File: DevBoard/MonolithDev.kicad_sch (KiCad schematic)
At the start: 4 parts

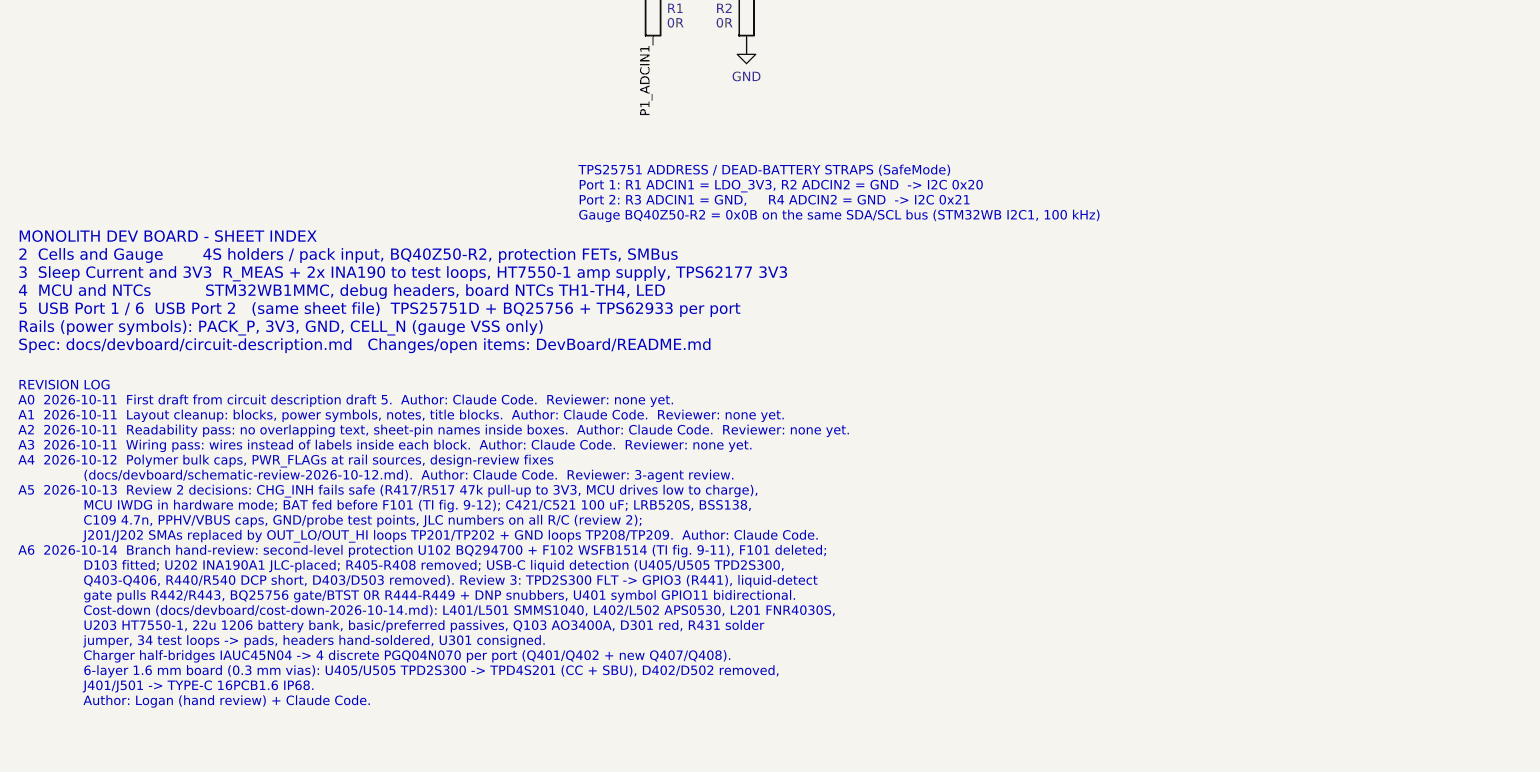
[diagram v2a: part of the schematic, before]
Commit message: Dev board schematic: tidy pass
- Title blocks on every sheet: rev A6, 2026-10-14, status line updated
  (was "Not reviewed, laid out, built or tested"); tidy_fields.py
  writes the same.
- Port sheet: the TPD4S201 block is titled with liquid detection
  ("CC/SBU PROTECTION (TPD4S201) + LIQUID DETECTION") and moved clear of
  the heading it collided with; I2Cc heading moved next to the EEPROM;
  PP5V heading clear of U405's GND.
- MCU sheet: test-point row out of the title block, with a heading;
  long NOTES lines wrapped inside the page border.
- Gauge sheet: cell-stack heading clear of its note; TP106 joins the
  test-point row.
- Top sheet: sheet index updated (BQ294700, TPD4S201, TH1-TH5) and
  spaced from the strap note and revision log; rev log line for the
  placement and this tidy.
- New tools/move_region.py moves a rectangle of a sheet (symbols,
  fields, wires, labels) by an offset.

Netlist identical before and after (265 nets); ERC 0 errors;
check_overlaps TOTAL 0.

Co-Authored-By: Claude Opus 5.5 <noreply@anthropic.com>
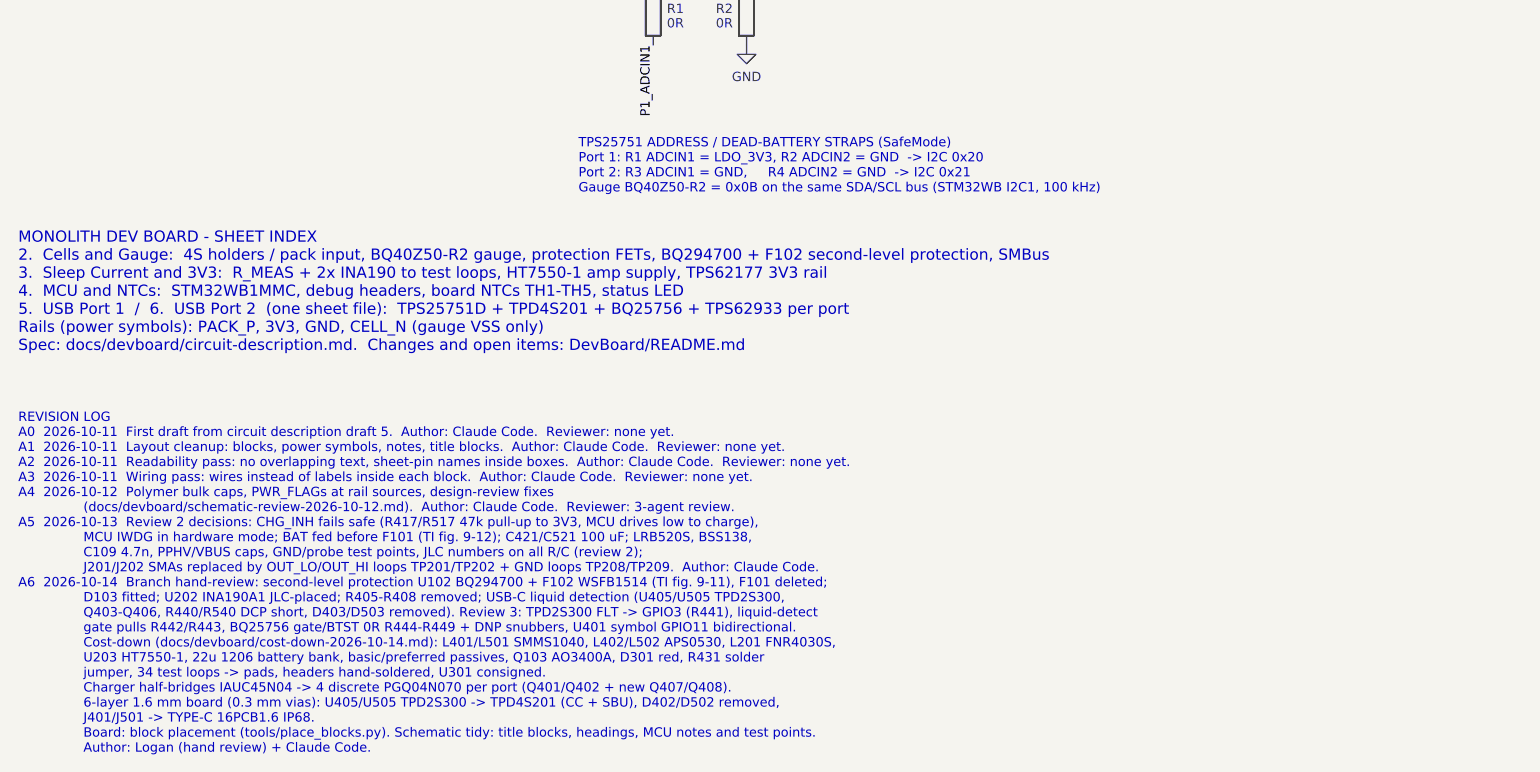
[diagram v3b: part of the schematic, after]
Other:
- note added: "MONOLITH DEV BOARD - SHEET INDEX 2. Cells and Gauge: 4S holders / pack input, BQ40Z50-R2 gauge, protection FETs, BQ294700 + F102 second-level protection, SMBus 3. Sleep Current and 3V3: R_MEAS + 2x INA190 to test loops, HT7550-1 amp supply, TPS62177 3V3 rail 4. MCU and NTCs: STM32WB1MMC, debug headers, board NTCs TH1-TH5, status LED 5. USB Port 1 / 6. USB Port 2 (one sheet file): TPS25751D + TPD4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"
- note removed: "MONOLITH DEV BOARD - SHEET INDEX 2 Cells and Gauge 4S holders / pack input, BQ40Z50-R2, protection FETs, SMBus 3 Sleep Current and 3V3 R_MEAS + 2x INA190 to test loops, HT7550-1 amp supply, TPS62177 3V3 4 MCU and NTCs STM32WB1MMC, debug headers, board NTCs TH1-TH4, LED 5 USB Port 1 / 6 USB Port 2 (same sheet file) TPS25751D + BQ25756 + TPS62933 per port Rails (power symbols): PACK_P, 3V3, GND, CE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"
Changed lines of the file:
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@@
 	(title_block
 		(title "Monolith dev board - top level")
-		(date "2026-10-11")
-		(rev "A (draft)")
+		(date "2026-10-14")
+		(rev "A6")
 		(company "Monolith 100 W battery bank - dev board")
 		(comment 1 "Sheet index, PD address straps")
 		(comment 2 "Spec + open items: DevBoard/README.md")
-		(comment 3 "Not reviewed, laid out, built or tested")
+		(comment 3 "Reviewed 3x (docs/devboard); board placed, not routed or built")
 	)
-	(text "MONOLITH DEV BOARD - SHEET INDEX\n2  Cells and Gauge        4S holders / pack input, BQ40Z50-R2, protection FETs, SMBus\n3  Sleep Current and 3V3  R_MEAS + 2x INA190 to test loops, HT7550-1 amp supply, TPS62177 3V3\n4  MCU and NTCs           STM32WB1MMC, debug headers, board NTCs TH1-TH4, LED\n5  USB Port 1 / 6  USB Port 2   (same sheet file)  TPS25751D + BQ25756 + TPS62933 per port\nRails (power symbols): PACK_P, 3V3, GND, CELL_N (gauge VSS only)\nSpec: docs/devboard/circuit-description.md   Changes/open items: DevBoard/README.md"
+	(text "MONOLITH DEV BOARD - SHEET INDEX\n2.  Cells and Gauge:  4S holders / pack input, BQ40Z50-R2 gauge, protection FETs, BQ294700 + F102 second-level protection, SMBus\n3.  Sleep Current and 3V3:  R_MEAS + 2x INA190 to test loops, HT7550-1 amp supply, TPS62177 3V3 rail\n4.  MCU and NTCs:  STM32WB1MMC, debug headers, board NTCs TH1-TH5, status LED\n5.  USB Port 1  /  6.  USB Port 2  (one sheet file):  TPS25751D + TPD4S201 + BQ25756 + TPS62933 per port\nRails (power symbols): PACK_P, 3V3, GND, CELL_N (gauge VSS only)\nSpec: docs/devboard/circuit-description.md.  Changes and open items: DevBoard/README.md"
 		(exclude_from_sim no)
 		(at 30.48 205.74 0)
@@
 		)
 	)
-	(text "REVISION LOG\nA0  2026-10-11  First draft from circuit description draft 5.  Author: Claude Code.  Reviewer: none yet.\nA1  2026-10-11  Layout cleanup: blocks, power symbols, notes, title blocks.  Author: Claude Code.  Reviewer: none yet.\nA2  2026-10-11  Readability pass: no overlapping text, sheet-pin names inside boxes.  Author: Claude Code.  Reviewer: none yet.\nA3  2026-10-11  Wiring pass: wires instead of labels inside each block.  Author: Claude Code.  Reviewer: none yet.\nA4  2026-10-12  Polymer bulk caps, PWR_FLAGs at rail sources, design-review fixes\n                (docs/devboard/schematic-review-2026-10-12.md).  Author: Claude Code.  Reviewer: 3-agent review.\nA5  2026-10-13  Review 2 decisions: CHG_INH fails safe (R417/R517 47k pull-up to 3V3, MCU drives low to charge),\n                MCU IWDG in hardware mode; BAT fed before F101 (TI fig. 9-12); C421/C521 100 uF; LRB520S, BSS138,\n                C109 4.7n, PPHV/VBUS caps, GND/probe test points, JLC numbers on all R/C (review 2);\n                J201/J202 SMAs replaced by OUT_LO/OUT_HI loops TP201/TP202 + GND loops TP208/TP209.  Author: Claude Code.\nA6  2026-10-14  Branch hand-review: second-level protection U102 BQ294700 + F102 WSFB1514 (TI fig. 9-11), F101 deleted;\n                D103 fitted; U202 INA190A1 JLC-placed; R405-R408 removed; USB-C liquid detection (U405/U505 TPD2S300,\n                Q403-Q406, R440/R540 DCP short, D403/D503 removed). Review 3: TPD2S300 FLT -> GPIO3 (R441), liquid-detect\n                gate pulls R442/R443, BQ25756 gate/BTST 0R R444-R449 + DNP snubbers, U401 symbol GPIO11 bidirectional.\n                Cost-down (docs/devboard/cost-down-2026-10-14.md): L401/L501 SMMS1040, L402/L502 APS0530, L201 FNR4030S,\n                U203 HT7550-1, 22u 1206 battery bank, basic/preferred passives, Q103 AO3400A, D301 red, R431 solder\n                jumper, 34 test loops -> pads, headers hand-soldered, U301 consigned.\n                Charger half-bridges IAUC45N04 -> 4 discrete PGQ04N070 per port (Q401/Q402 + new Q407/Q408).\n                6-layer 1.6 mm board (0.3 mm vias): U405/U505 TPD2S300 -> TPD4S201 (CC + SBU), D402/D502 removed,\n                J401/J501 -> TYPE-C 16PCB1.6 IP68.\n                Author: Logan (hand review) + Claude Code."
+	(text "REVISION LOG\nA0  2026-10-11  First draft from circuit description draft 5.  Author: Claude Code.  Reviewer: none yet.\nA1  2026-10-11  Layout cleanup: blocks, power symbols, notes, title blocks.  Author: Claude Code.  Reviewer: none yet.\nA2  2026-10-11  Readability pass: no overlapping text, sheet-pin names inside boxes.  Author: Claude Code.  Reviewer: none yet.\nA3  2026-10-11  Wiring pass: wires instead of labels inside each block.  Author: Claude Code.  Reviewer: none yet.\nA4  2026-10-12  Polymer bulk caps, PWR_FLAGs at rail sources, design-review fixes\n                (docs/devboard/schematic-review-2026-10-12.md).  Author: Claude Code.  Reviewer: 3-agent review.\nA5  2026-10-13  Review 2 decisions: CHG_INH fails safe (R417/R517 47k pull-up to 3V3, MCU drives low to charge),\n                MCU IWDG in hardware mode; BAT fed before F101 (TI fig. 9-12); C421/C521 100 uF; LRB520S, BSS138,\n                C109 4.7n, PPHV/VBUS caps, GND/probe test points, JLC numbers on all R/C (review 2);\n                J201/J202 SMAs replaced by OUT_LO/OUT_HI loops TP201/TP202 + GND loops TP208/TP209.  Author: Claude Code.\nA6  2026-10-14  Branch hand-review: second-level protection U102 BQ294700 + F102 WSFB1514 (TI fig. 9-11), F101 deleted;\n                D103 fitted; U202 INA190A1 JLC-placed; R405-R408 removed; USB-C liquid detection (U405/U505 TPD2S300,\n                Q403-Q406, R440/R540 DCP short, D403/D503 removed). Review 3: TPD2S300 FLT -> GPIO3 (R441), liquid-detect\n                gate pulls R442/R443, BQ25756 gate/BTST 0R R444-R449 + DNP snubbers, U401 symbol GPIO11 bidirectional.\n                Cost-down (docs/devboard/cost-down-2026-10-14.md): L401/L501 SMMS1040, L402/L502 APS0530, L201 FNR4030S,\n                U203 HT7550-1, 22u 1206 battery bank, basic/preferred passives, Q103 AO3400A, D301 red, R431 solder\n                jumper, 34 test loops -> pads, headers hand-soldered, U301 consigned.\n                Charger half-bridges IAUC45N04 -> 4 discrete PGQ04N070 per port (Q401/Q402 + new Q407/Q408).\n                6-layer 1.6 mm board (0.3 mm vias): U405/U505 TPD2S300 -> TPD4S201 (CC + SBU), D402/D502 removed,\n                J401/J501 -> TYPE-C 16PCB1.6 IP68.\n                Board: block placement (tools/place_blocks.py). Schematic tidy: title blocks, headings, MCU notes and test points.\n                Author: Logan (hand review) + Claude Code."
 		(exclude_from_sim no)
-		(at 30.48 254.0 0)
+		(at 30.48 260.35 0)
 		(effects
 			(font
@@
 	(text "TPS25751 ADDRESS / DEAD-BATTERY STRAPS (SafeMode)\nPort 1: R1 ADCIN1 = LDO_3V3, R2 ADCIN2 = GND  -> I2C 0x20\nPort 2: R3 ADCIN1 = GND,     R4 ADCIN2 = GND  -> I2C 0x21\nGauge BQ40Z50-R2 = 0x0B on the same SDA/SCL bus (STM32WB I2C1, 100 kHz)"
 		(exclude_from_sim no)
-		(at 106.68 187.96 0)
+		(at 106.68 184.15 0)
 		(effects
 			(font

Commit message: Dev board rev A7: CC2340R5MODA MCU, TMP1075 sensors, shared IRQ_N
- U301 STM32WB1MMC -> TI CC2340R5MODA (cost-down; BLE only, on-chip OTA).
  New symbol and footprint (MHA0024A, with the fig. 9-2 antenna keep-out),
  RF match C313/R321/C314/C315, RSTN pull-up R302, wired per SWRS349A fig. 9-1.
- Only 10 usable GPIOs, so the five board NTCs become TMP1075 I2C sensors:
  U302-U304 fitted (port 1 stage, port 2 stage, connectors), U305/U306 DNP.
  FET over-temperature moves to the gauge internal sensor.
- TPS25751 IRQs, gauge BTP and TMP1075 ALERTs share one open-drain IRQ_N
  (R314 pull-up; R315, R114 DNP).
- R313 fitted at 470k: CC2340 pins float in reset, so it keeps the 3V3 rail
  out of sleep mode during boot.
- Pin budget doc, circuit description, bring-up checklist and README item 40
  updated; mcu-io-power-states.md flagged for rewrite. PCB not updated yet.

Co-Authored-By: Claude Opus 5.5 <noreply@anthropic.com>
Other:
- note added: "MONOLITH DEV BOARD - SHEET INDEX 2. Cells and Gauge: 4S holders / pack input, BQ40Z50-R2 gauge, protection FETs, BQ294700 + F102 second-level protection, SMBus 3. Sleep Current and 3V3: R_MEAS + 2x INA190 to test loops, HT7550-1 amp supply, TPS62177 3V3 rail 4. MCU and NTCs: CC2340R5MODA, debug headers, TMP1075 board temperature sensors, status LED 5. USB Port 1 / 6. USB Port 2 (one sheet file): 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"
- note removed: "MONOLITH DEV BOARD - SHEET INDEX 2. Cells and Gauge: 4S holders / pack input, BQ40Z50-R2 gauge, protection FETs, BQ294700 + F102 second-level protection, SMBus 3. Sleep Current and 3V3: R_MEAS + 2x INA190 to test loops, HT7550-1 amp supply, TPS62177 3V3 rail 4. MCU and NTCs: STM32WB1MMC, debug headers, board NTCs TH1-TH5, status LED 5. USB Port 1 / 6. USB Port 2 (one sheet file): TPS25751D + TPD4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"
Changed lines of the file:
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@@
 		(comment 3 "Reviewed 3x (docs/devboard); board placed, not routed or built")
 	)
-	(text "MONOLITH DEV BOARD - SHEET INDEX\n2.  Cells and Gauge:  4S holders / pack input, BQ40Z50-R2 gauge, protection FETs, BQ294700 + F102 second-level protection, SMBus\n3.  Sleep Current and 3V3:  R_MEAS + 2x INA190 to test loops, HT7550-1 amp supply, TPS62177 3V3 rail\n4.  MCU and NTCs:  STM32WB1MMC, debug headers, board NTCs TH1-TH5, status LED\n5.  USB Port 1  /  6.  USB Port 2  (one sheet file):  TPS25751D + TPD4S201 + BQ25756 + TPS62933 per port\nRails (power symbols): PACK_P, 3V3, GND, CELL_N (gauge VSS only)\nSpec: docs/devboard/circuit-description.md.  Changes and open items: DevBoard/README.md"
+	(text "MONOLITH DEV BOARD - SHEET INDEX\n2.  Cells and Gauge:  4S holders / pack input, BQ40Z50-R2 gauge, protection FETs, BQ294700 + F102 second-level protection, SMBus\n3.  Sleep Current and 3V3:  R_MEAS + 2x INA190 to test loops, HT7550-1 amp supply, TPS62177 3V3 rail\n4.  MCU and NTCs:  CC2340R5MODA, debug headers, TMP1075 board temperature sensors, status LED\n5.  USB Port 1  /  6.  USB Port 2  (one sheet file):  TPS25751D + TPD4S201 + BQ25756 + TPS62933 per port\nRails (power symbols): PACK_P, 3V3, GND, CELL_N (gauge VSS only)\nSpec: docs/devboard/circuit-description.md.  Changes and open items: DevBoard/README.md"
 		(exclude_from_sim no)
 		(at 30.48 205.74 0)
@@
 		)
 	)
-	(global_label "IRQ1"
+	(global_label "IRQ_N"
 		(shape bidirectional)
 		(at 90 104.14 0)
@@
 		)
 	)
-	(global_label "IRQ2"
+	(global_label "IRQ_N"
 		(shape bidirectional)
 		(at 220 104.14 0)
